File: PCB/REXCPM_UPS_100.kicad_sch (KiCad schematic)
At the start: 9 parts, among them J1 Model_100_System_BUS, J2 SM04B, U1 742G02

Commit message: batt footprint
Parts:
- J1: footprint 000_LOCAL:DIP-40_pins -> 000_LOCAL:DIP-40_PCB
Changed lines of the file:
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@@
   (title_block
     (title "REXCPM_UPS_100")
-    (date "2023-09-21")
-    (rev "004")
+    (date "2023-11-04")
+    (rev "005")
     (company "Brian K. White - b.kenyon.w@gmail.com")
     (comment 1 "Replacement REXCPM system bus interface with memory battery")
@@
       (effects (font (size 1.27 1.27)))
     )
-    (property "Footprint" "000_LOCAL:DIP-40_pins" (at 76.2 69.85 0)
+    (property "Footprint" "000_LOCAL:DIP-40_PCB" (at 76.2 69.85 0)
       (effects (font (size 1.27 1.27)) hide)
     )

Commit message: silkscreen
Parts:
- U1: value 742G02 -> 2G02
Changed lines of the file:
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@@
       (effects (font (size 1.27 1.27)))
     )
-    (property "Value" "742G02" (at 144.78 93.98 0)
+    (property "Value" "2G02" (at 144.78 93.98 0)
       (effects (font (size 1.27 1.27)))
     )
@@
       (effects (font (size 1.27 1.27)))
     )
-    (property "Value" "742G02" (at 115.57 91.44 0)
+    (property "Value" "2G02" (at 115.57 91.44 0)
       (effects (font (size 1.27 1.27)))
     )
@@
       (effects (font (size 1.27 1.27)) (justify left))
     )
-    (property "Value" "742G02" (at 139.7 179.07 0)
+    (property "Value" "2G02" (at 139.7 179.07 0)
       (effects (font (size 1.27 1.27)) (justify left))
     )

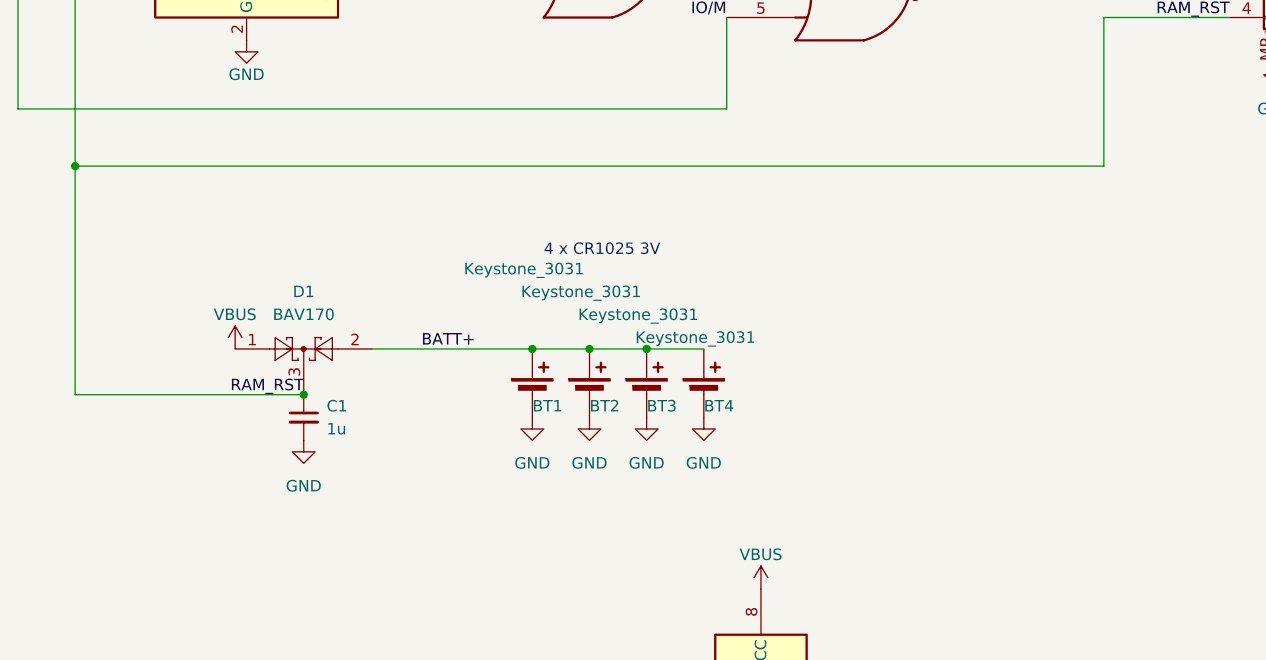
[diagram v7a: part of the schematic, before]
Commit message: move 1u cap from RAMRST to VBUS
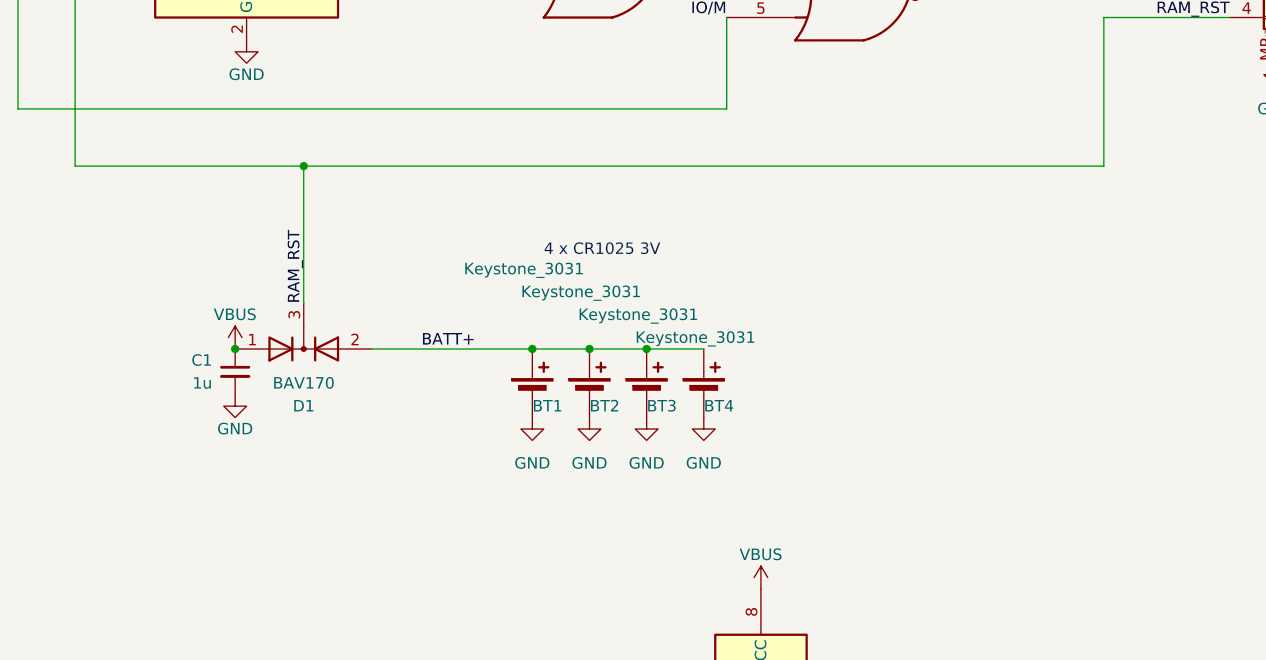
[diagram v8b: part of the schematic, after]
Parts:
- D1: symbol 000_LOCAL:BAT54C -> 000_LOCAL:BAV170
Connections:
- net RAM_RST: no longer C1.1
- net VBUS: now also C1.1
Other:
- moved on the sheet: C1
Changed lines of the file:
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@@
   (title_block
     (title "REXCPM_UPS_100")
-    (date "2023-11-04")
-    (rev "005")
+    (date "2023-11-20")
+    (rev "006")
     (company "Brian K. White - b.kenyon.w@gmail.com")
     (comment 1 "Replacement REXCPM system bus interface with memory battery")
@@
   (junction (at 107.95 140.97) (diameter 0) (color 0 0 0 0)
   )
-  (junction (at 82.55 146.05) (diameter 0) (color 0 0 0 0)
-  )
   (junction (at 114.3 140.97) (diameter 0) (color 0 0 0 0)
   )
   (junction (at 101.6 101.6) (diameter 0) (color 0 0 0 0)
   )
-  (junction (at 57.15 120.65) (diameter 0) (color 0 0 0 0)
+  (junction (at 82.55 120.65) (diameter 0) (color 0 0 0 0)
   )
   (junction (at 120.65 140.97) (diameter 0) (color 0 0 0 0)
+  )
+  (junction (at 74.93 140.97) (diameter 0) (color 0 0 0 0)
   )
   (no_connect (at 88.9 96.52))
@@
     (stroke (width 0) (type default))
   )
-  (wire (pts (xy 57.15 146.05) (xy 82.55 146.05))
+  (wire (pts (xy 82.55 120.65) (xy 82.55 135.89))
     (stroke (width 0) (type default))
   )
@@
     (stroke (width 0) (type default))
   )
-  (wire (pts (xy 57.15 120.65) (xy 171.45 120.65))
+  (wire (pts (xy 57.15 120.65) (xy 82.55 120.65))
     (stroke (width 0) (type default))
   )
@@
     (stroke (width 0) (type default))
   )
-  (wire (pts (xy 57.15 120.65) (xy 57.15 146.05))
-    (stroke (width 0) (type default))
-  )
   (wire (pts (xy 129.54 104.14) (xy 129.54 114.3))
     (stroke (width 0) (type default))
@@
   )
   (wire (pts (xy 101.6 96.52) (xy 101.6 101.6))
+    (stroke (width 0) (type default))
+  )
+  (wire (pts (xy 82.55 120.65) (xy 171.45 120.65))
     (stroke (width 0) (type default))
   )
@@
     (effects (font (size 1.27 1.27)) (justify right bottom))
   )
-  (label "RAM_RST" (at 82.55 146.05 180) (fields_autoplaced)
-    (effects (font (size 1.27 1.27)) (justify right bottom))
+  (label "RAM_RST" (at 82.55 135.89 90) (fields_autoplaced)
+    (effects (font (size 1.27 1.27)) (justify left bottom))
   )
   (label "RAM" (at 157.48 101.6 0) (fields_autoplaced)
@@
     )
   )
-  (symbol (lib_id "000_LOCAL:BAT54C") (at 82.55 140.97 0) (unit 1)
-    (in_bom yes) (on_board yes) (dnp no)
-    (property "Reference" "D1" (at 82.55 134.62 0)
-      (effects (font (size 1.27 1.27)))
-    )
-    (property "Value" "BAV170" (at 82.55 137.16 0)
-      (effects (font (size 1.27 1.27)))
-    )
-    (property "Footprint" "000_LOCAL:SOT-23" (at 84.455 137.795 0)
-      (effects (font (size 1.27 1.27)) (justify left) hide)
-    )
-    (property "Datasheet" "datasheets/BAV170.pdf" (at 80.518 140.97 0)
+  (symbol (lib_id "000_LOCAL:BAV170") (at 82.55 140.97 0) (mirror x) (unit 1)
+    (in_bom yes) (on_board yes) (dnp no)
+    (property "Reference" "D1" (at 82.55 147.32 0)
+      (effects (font (size 1.27 1.27)))
+    )
+    (property "Value" "BAV170" (at 82.55 144.78 0)
+      (effects (font (size 1.27 1.27)))
+    )
+    (property "Footprint" "000_LOCAL:SOT-23" (at 82.55 140.97 0)
+      (effects (font (size 1.27 1.27)) hide)
+    )
+    (property "Datasheet" "datasheets/BAV170.pdf" (at 82.55 140.97 0)
       (effects (font (size 1.27 1.27)) hide)
     )
@@
     )
   )
-  (symbol (lib_id "000_LOCAL:C") (at 82.55 148.59 0) (unit 1)
-    (in_bom yes) (on_board yes) (dnp no) (fields_autoplaced)
-    (property "Reference" "C1" (at 85.09 147.3263 0)
-      (effects (font (size 1.27 1.27)) (justify left))
-    )
-    (property "Value" "1u" (at 85.09 149.8663 0)
-      (effects (font (size 1.27 1.27)) (justify left))
-    )
-    (property "Footprint" "000_LOCAL:C_0805" (at 82.55 148.59 0)
-      (effects (font (size 1.27 1.27)) hide)
-    )
-    (property "Datasheet" "~" (at 82.55 148.59 0)
+  (symbol (lib_id "000_LOCAL:C") (at 74.93 143.51 0) (unit 1)
+    (in_bom yes) (on_board yes) (dnp no)
+    (property "Reference" "C1" (at 72.39 142.24 0)
+      (effects (font (size 1.27 1.27)) (justify right))
+    )
+    (property "Value" "1u" (at 72.39 144.78 0)
+      (effects (font (size 1.27 1.27)) (justify right))
+    )
+    (property "Footprint" "000_LOCAL:C_0805" (at 74.93 143.51 0)
+      (effects (font (size 1.27 1.27)) hide)
+    )
+    (property "Datasheet" "~" (at 74.93 143.51 0)
       (effects (font (size 1.27 1.27)) hide)
     )
@@
     )
   )
-  (symbol (lib_name "GND_1") (lib_id "power:GND") (at 82.55 151.13 0) (unit 1)
-    (in_bom yes) (on_board yes) (dnp no) (fields_autoplaced)
-    (property "Reference" "#PWR09" (at 82.55 157.48 0)
-      (effects (font (size 1.27 1.27)) hide)
-    )
-    (property "Value" "GND" (at 82.55 156.21 0)
-      (effects (font (size 1.27 1.27)))
-    )
-    (property "Footprint" "" (at 82.55 151.13 0)
-      (effects (font (size 1.27 1.27)) hide)
-    )
-    (property "Datasheet" "" (at 82.55 151.13 0)
-      (effects (font (size 1.27 1.27)) hide)
-    )
+  (symbol (lib_name "GND_1") (lib_id "power:GND") (at 74.93 146.05 0) (unit 1)
+    (in_bom yes) (on_board yes) (dnp no)
+    (property "Reference" "#PWR09" (at 74.93 152.4 0)
+      (effects (font (size 1.27 1.27)) hide)
+    )
+    (property "Value" "GND" (at 74.93 149.86 0)
+      (effects (font (size 1.27 1.27)))
+    )
+    (property "Footprint" "" (at 74.93 146.05 0)
+      (effects (font (size 1.27 1.27)) hide)
+    )
+    (property "Datasheet" "" (at 74.93 146.05 0)
+      (effects (font (size 1.27 1.27)) hide)
+    )
